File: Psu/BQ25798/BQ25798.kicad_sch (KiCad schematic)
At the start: 46 parts, among them J1 I2C, J2 IN, J3 UPS, J4 CTRL, J5 BAT, Q1 NMOS, Q2 NMOS, Q3 NMOS, U1 BQ25798

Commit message: Production Values
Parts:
- R8: value 5.24k -> 5.2k; footprint Resistor_SMD:R_0603_1608Metric -> Resistor_SMD:R_0805_2012Metric
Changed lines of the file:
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@@
 			)
 		)
-		(property "Value" "5.24k"
+		(property "Value" "5.2k"
 			(at 106.68 138.4299 0)
 			(show_name no)
@@
 			)
 		)
-		(property "Footprint" "Resistor_SMD:R_0603_1608Metric"
+		(property "Footprint" "Resistor_SMD:R_0805_2012Metric"
 			(at 109.22 137.16 0)
 			(hide yes)

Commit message: YARR
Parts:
- removed J1: I2C, Connector_PinHeader_2.54mm:PinHeader_1x02_P2.54mm_Vertical, symbol Connector:Conn_01x02_Pin
- removed J4: CTRL, Connector_PinHeader_2.54mm:PinHeader_1x03_P2.54mm_Vertical, symbol Connector:Conn_01x03_Pin
- added C25, C26: 10 uF, Capacitor_SMD:C_0603_1608Metric, symbol Device:C_Small
- added C27, C28: 100nF, Capacitor_SMD:C_0805_2012Metric, symbol Device:C_Small
- added J6: USB_C_Receptacle_USB2.0, Connector_USB:USB_C_Receptacle_HRO_TYPE-C-31-M-12, symbol Connector:USB_C_Receptacle_USB2.0
- added R10, R11: 5.1k, Resistor_SMD:R_0603_1608Metric, symbol Device:R
- added R12: 10k Ohm, Resistor_SMD:R_0805_2012Metric, symbol Device:R
- added R13, R14: 22, Resistor_SMD:R_0603_1608Metric, symbol Device:R
- added SW1: KH-6X6X5H-STM, footprints:KH-6X6X5H-STM_SKE, symbol Personal:KH-6X6X5H-STM
- added U2: CH552G, footprints:CH552G, symbol Personal:CH552G
- added U3: AMS1117-3.3, Package_TO_SOT_SMD:SOT-223-3_TabPin2, symbol Regulator_Linear:AMS1117-3.3
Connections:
- net GND: now also C25.2, C26.2, C27.1, C28.1, J6.A1 (GND), J6.A12 (GND), J6.B1 (GND), J6.B12 (GND), J6.S1 (SHIELD), R10.1, R11.2, R12.1, U2.14 (GND), U3.1 (GND)
- net VIN: now reaches C2.1, J2.1 (Pin_1), Q1.1 (D), R2.1, U1.9 (VAC1)
- net VIN: now also C25.1, U3.3 (VI)
- net at U1.14 (SCL): now also U2.11 (P3.4)
- net at U1.15 (SDA): now also U2.10 (P3.3)
- net at U1.21 (~{INT}): now also U2.9 (P1.1)
- net at U1.13 (~{CE}): now also U2.7 (P3.1)
- net at U1.12 (~{QON}): now also U2.8 (P3.0)
- new net: R12.2, SW1.A
- new net: SW1.B, U2.6 (RST)
- new net: J6.A6 (D+), J6.B6 (D+), R14.1
- new net: J6.A5 (CC1), R10.2
- new net: J6.A7 (D-), J6.B7 (D-), R13.1
- new net: J6.B5 (CC2), R11.1
- new net: J6.A4 (VBUS), J6.A9 (VBUS), J6.B4 (VBUS), J6.B9 (VBUS)
- new net +3V3: C26.1, C27.2, C28.2, SW1.C, SW1.D, U2.15 (VCC), U2.16 (3V3), U3.2 (VO)
- new net D+: R14.2, U2.12 (P3.6)
- new net D-: R13.2, U2.13 (P3.7)
- no-connect marks 2 -> 10

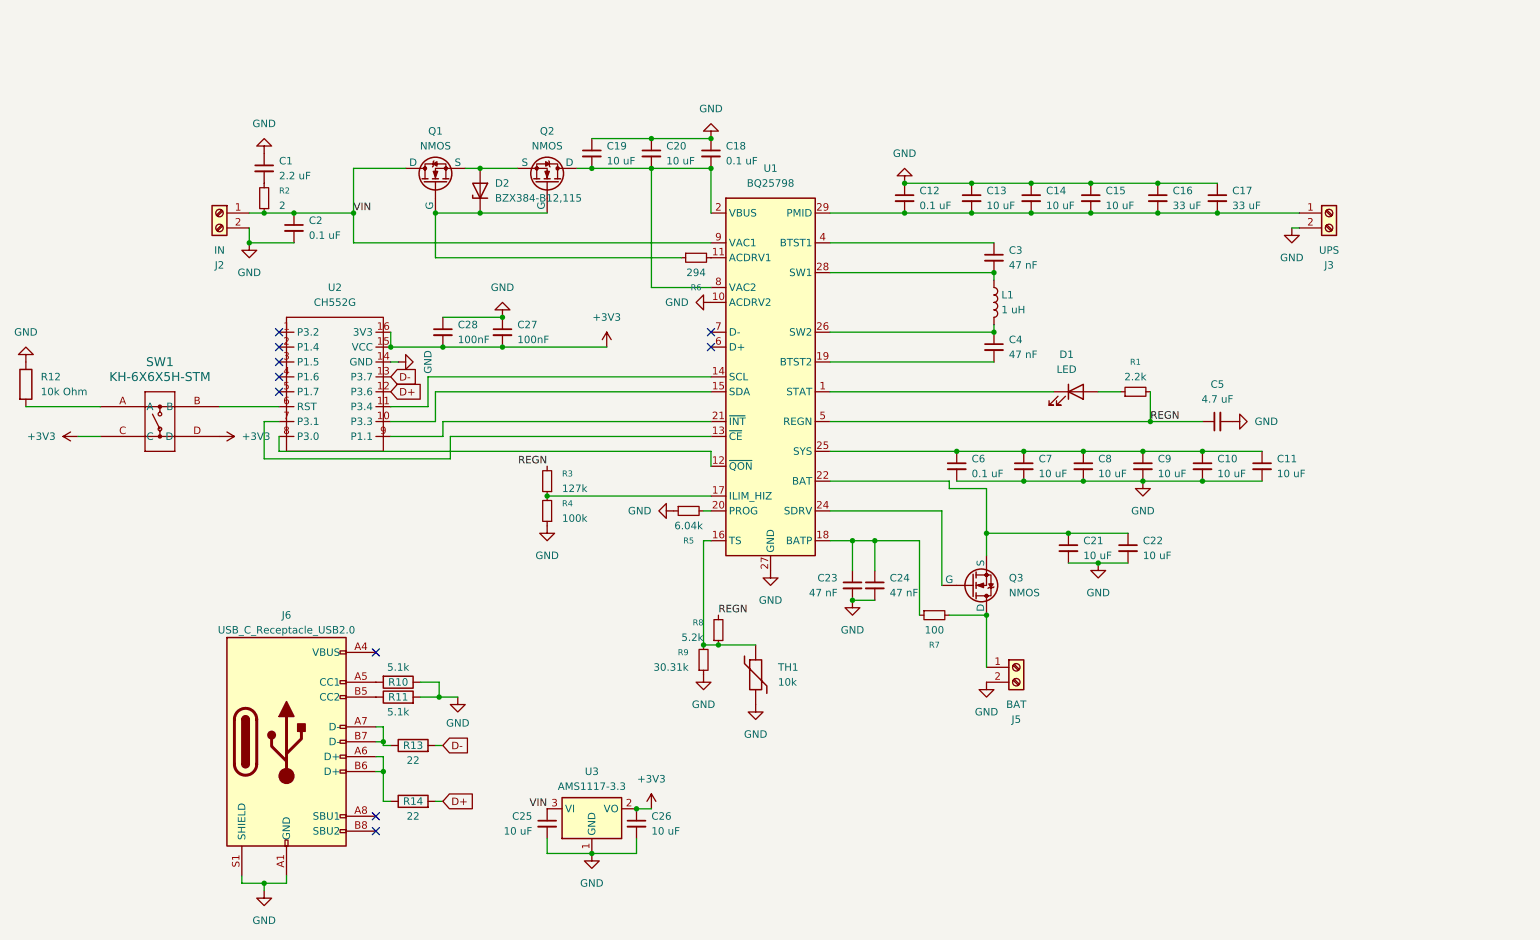
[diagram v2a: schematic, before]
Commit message: Rework some trace lines for wider with in high amperage environments
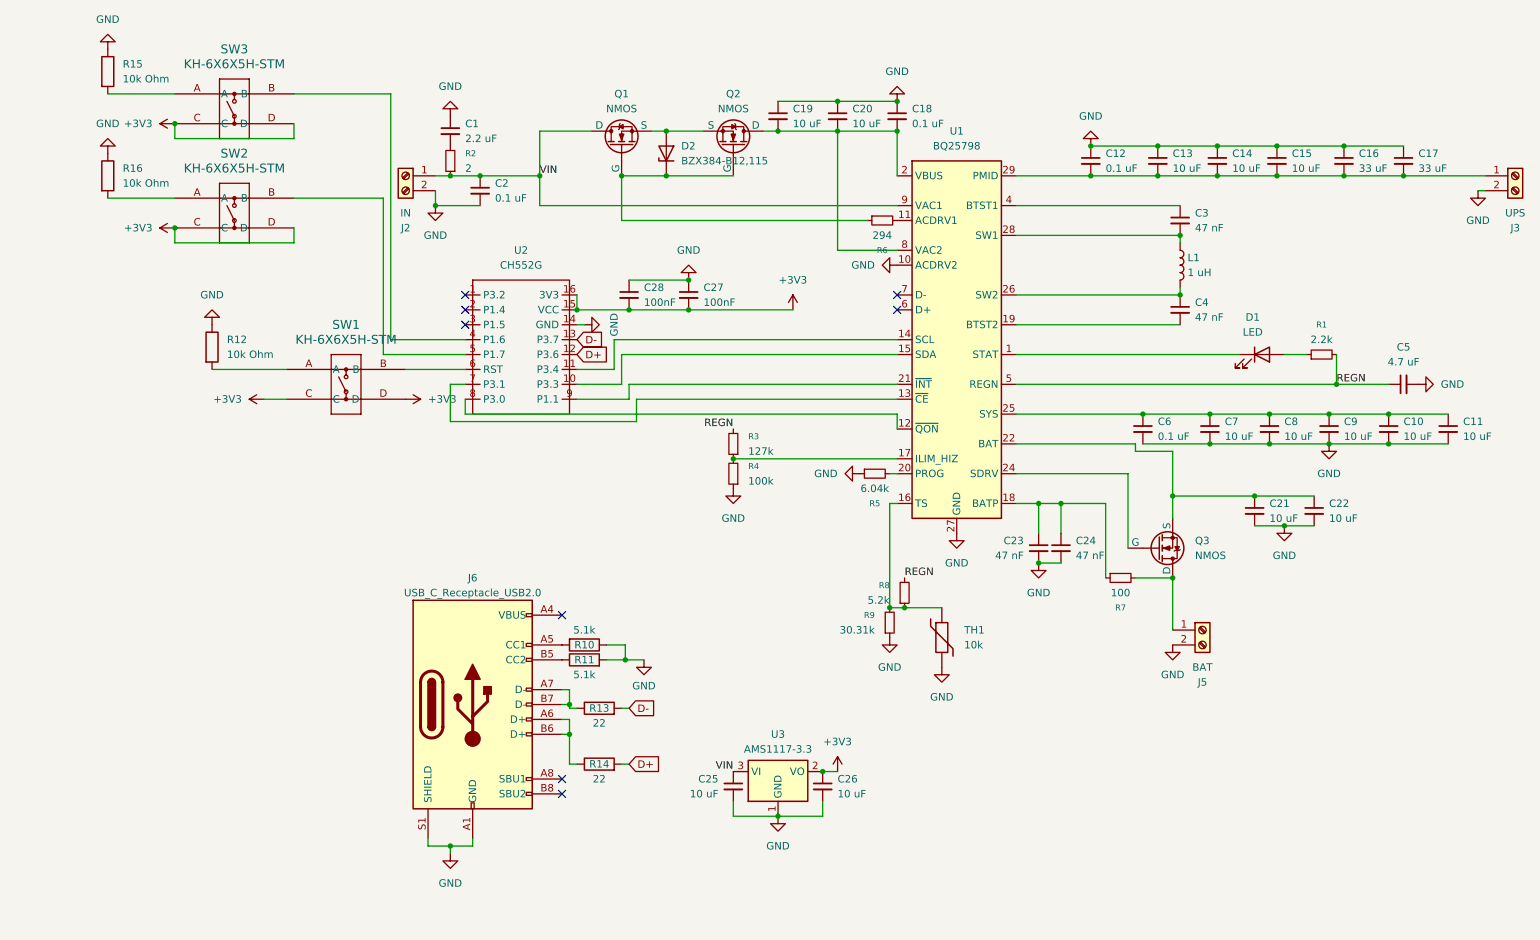
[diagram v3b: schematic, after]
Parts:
- added R15, R16: 10k Ohm, Resistor_SMD:R_0805_2012Metric, symbol Device:R
- added SW2, SW3: KH-6X6X5H-STM, footprints:KH-6X6X5H-STM_SKE, symbol Personal:KH-6X6X5H-STM
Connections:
- net +3V3: now also SW2.C, SW2.D, SW3.C, SW3.D
- net GND: now also R15.1, R16.1
- net at U2.4 (P1.6): now also SW3.B
- net at U2.5 (P1.7): now also SW2.B
- new net: R16.2, SW2.A
- new net: R15.2, SW3.A
- no-connect marks 10 -> 8
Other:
- moved on the sheet: C1, C10, C11, C12, C13, C14, C15, C16, C17, C18, C19, C2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
